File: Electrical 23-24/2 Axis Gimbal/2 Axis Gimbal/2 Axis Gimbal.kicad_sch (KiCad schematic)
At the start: 28 parts, among them IC1 BNO085, IC2 AP1086DL-13, J1 Conn_01x06_Socket, J2 Conn_01x06_Socket, U1 ATtiny404-SS

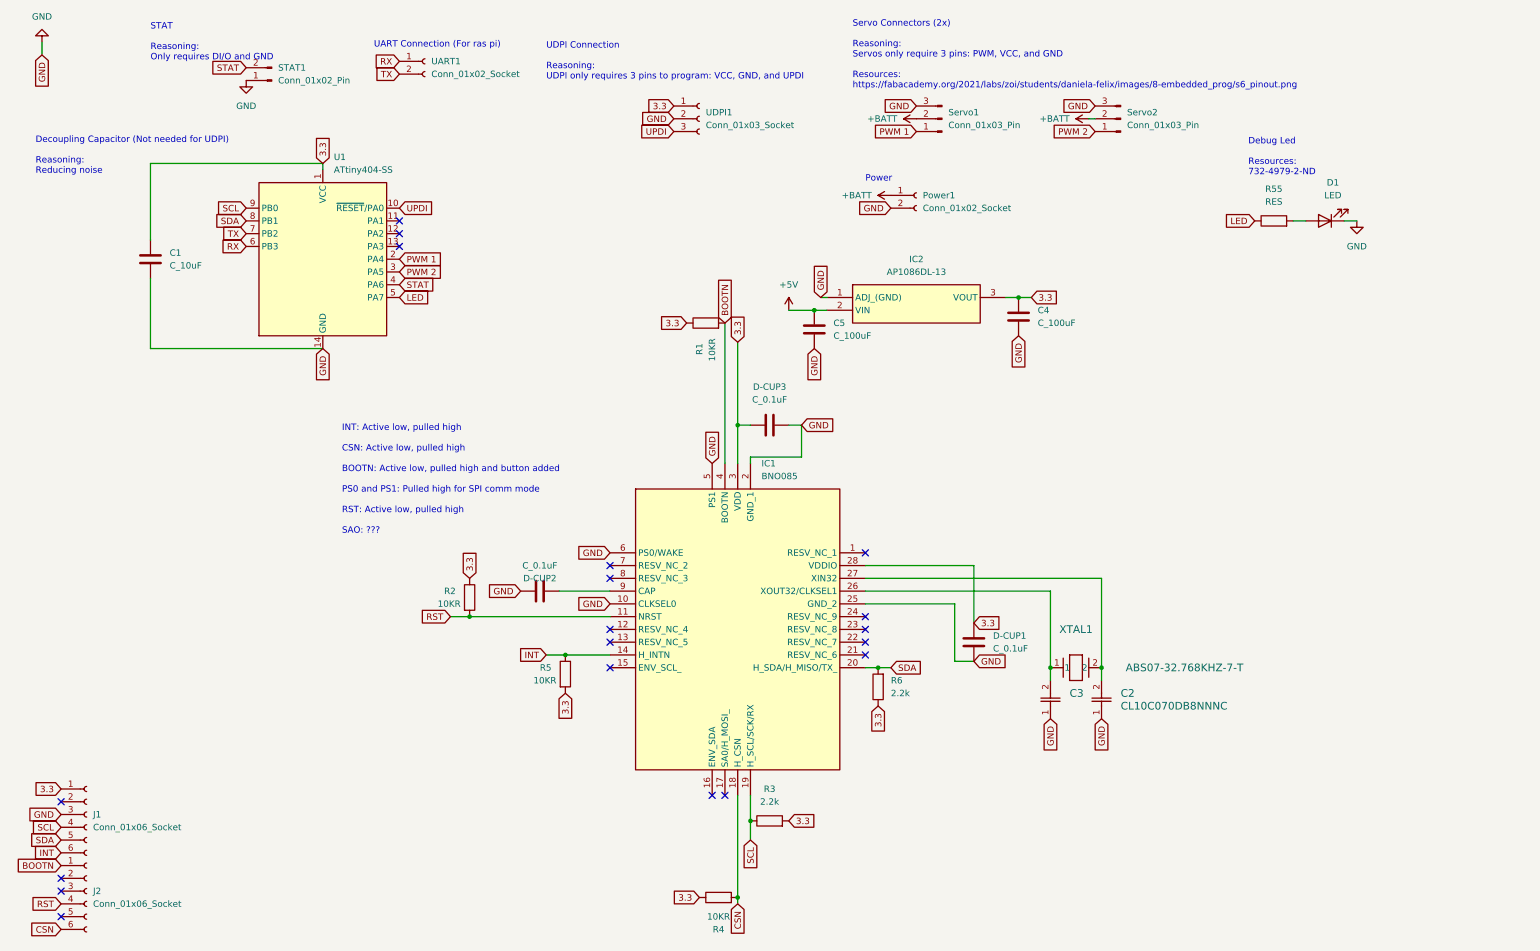
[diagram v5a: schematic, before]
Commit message: Fix gimbal schematic
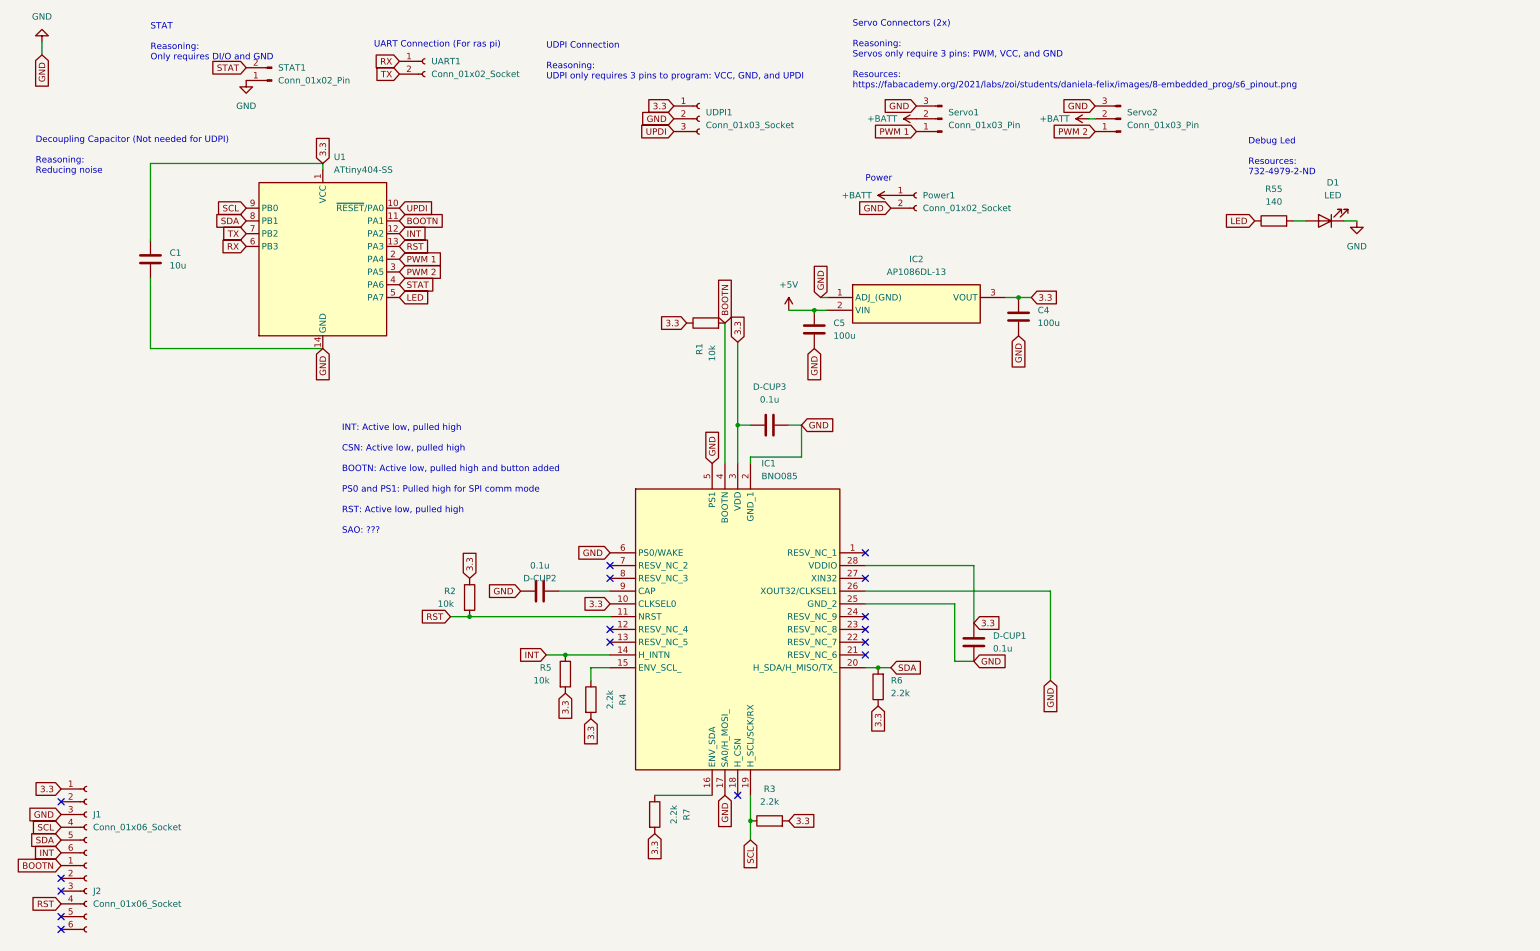
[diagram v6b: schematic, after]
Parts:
- removed C2, C3: CL10C070DB8NNNC, Capacitor_SMD:C_0201_0603Metric_Pad0.64x0.40mm_HandSolder, symbol 7pf:CL10C070DB8NNNC
- removed R4: 10KR, Resistor_SMD:R_0603_1608Metric_Pad0.98x0.95mm_HandSolder, symbol oem:10KR
- removed XTAL1: ABS07-32.768KHZ-7-T, 32Crys:XTAL_ABS07-32.768KHZ-7-T_ABR, symbol 32Crys:ABS07-32.768KHZ-7-T
- added R4, R7: 2.2k, Resistor_SMD:R_1206_3216Metric_Pad1.30x1.75mm_HandSolder, symbol Device:R
- C1: value C_10uF -> 10u
- C4, C5: value C_100uF -> 100u
- D-CUP1, D-CUP2, D-CUP3: value C_0.1uF -> 0.1u
- R1, R2, R5: value 10KR -> 10k
- R55: value RES -> 140
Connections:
- net 3.3: now also IC1.10 (CLKSEL0), R4.2, R7.2
- net BOOTN: now also U1.11 (PA1)
- net GND: now also IC1.17 (SA0/H_MOSI_), IC1.26 (XOUT32/CLKSEL1); no longer IC1.10 (CLKSEL0)
- net INT: now also U1.12 (PA2)
- net RST: now also U1.13 (PA3)
- net at IC1.15 (ENV_SCL_): now also R4.1
- net at IC1.16 (ENV_SDA): now also R7.1
- net CSN: no longer names the net of J2.6 (Pin_6)
- net CSN: no longer IC1.18 (H_CSN)
- no-connect marks 19 -> 16

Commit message: Finished Gimbal Board
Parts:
- removed J1, J2: Conn_01x06_Socket, Connector_PinHeader_2.54mm:PinHeader_1x06_P2.54mm_Vertical, symbol Connector:Conn_01x06_Socket
- removed UDPI1: Conn_01x03_Socket, Connector_PinSocket_2.54mm:PinSocket_1x03_P2.54mm_Vertical, symbol Connector:Conn_01x03_Socket
- added Servo3: Conn_01x03_Pin, Connector_JST:JST_XH_B3B-XH-A_1x03_P2.50mm_Vertical, symbol Connector:Conn_01x03_Pin
- added U2: ~, gimbal:breakout, symbol gimbal:breakout
- added UDPI1: Conn_01x03_Socket, Connector_PinSocket_2.54mm:PinSocket_1x05_P2.54mm_Vertical, symbol Connector:Conn_01x05_Socket
- C1: footprint Capacitor_SMD:C_0805_2012Metric_Pad1.18x1.45mm_HandSolder -> Capacitor_SMD:C_0603_1608Metric_Pad1.08x0.95mm_HandSolder
- C2: renamed from D-CUP2; footprint Capacitor_SMD:C_0402_1005Metric_Pad0.74x0.62mm_HandSolder -> Capacitor_SMD:C_0603_1608Metric_Pad1.08x0.95mm_HandSolder
- C3: renamed from D-CUP3; footprint Capacitor_SMD:C_0402_1005Metric_Pad0.74x0.62mm_HandSolder -> Capacitor_SMD:C_0603_1608Metric_Pad1.08x0.95mm_HandSolder
- C4, C5: value 100u -> 10u; footprint Capacitor_SMD:C_1206_3216Metric_Pad1.33x1.80mm_HandSolder -> Capacitor_SMD:C_0603_1608Metric_Pad1.08x0.95mm_HandSolder
- C6: renamed from D-CUP1; footprint Capacitor_SMD:C_0402_1005Metric_Pad0.74x0.62mm_HandSolder -> Capacitor_SMD:C_0603_1608Metric_Pad1.08x0.95mm_HandSolder
- IC1: footprint BNO085:BNO085 -> gimbal:BNO085
- IC2: footprint VReg3.3:TO252-3L_1 -> gimbal:TO252-3L_1
- Power1, UART1: footprint Connector_PinSocket_2.54mm:PinSocket_1x02_P2.54mm_Vertical -> Connector_JST:JST_XH_B2B-XH-A_1x02_P2.50mm_Vertical
- R1: footprint Resistor_SMD:R_0201_0603Metric_Pad0.64x0.40mm_HandSolder -> Resistor_SMD:R_0603_1608Metric_Pad0.98x0.95mm_HandSolder
- R3, R4, R6, R7: footprint Resistor_SMD:R_1206_3216Metric_Pad1.30x1.75mm_HandSolder -> Resistor_SMD:R_0603_1608Metric_Pad0.98x0.95mm_HandSolder
- R55: footprint LED_SMD:LED_1206_3216Metric_Pad1.42x1.75mm_HandSolder -> Resistor_SMD:R_0603_1608Metric_Pad0.98x0.95mm_HandSolder
- STAT1: footprint Connector_PinHeader_2.54mm:PinHeader_1x02_P2.54mm_Vertical -> Connector_JST:JST_XH_B2B-XH-A_1x02_P2.50mm_Vertical
- Servo1, Servo2: footprint Connector_PinHeader_2.54mm:PinHeader_1x03_P2.54mm_Vertical -> Connector_JST:JST_XH_B3B-XH-A_1x03_P2.50mm_Vertical
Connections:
- net +5V is gone; now on net +BATT: C5.1, IC2.2 (VIN)
- net +BATT: now also Servo3.2 (Pin_2)
- net 3.3: now also U2.1 (Vin), UDPI1.2 (Pin_2)
- net BOOTN: now also U2.12 (BT)
- net GND: now also Servo3.3 (Pin_3), U2.10 (P0), U2.11 (P1), U2.3 (GND), UDPI1.3 (Pin_3)
- net INT: now also U2.6 (Int)
- net PWM 1: now also U1.13 (PA3); no longer U1.2 (PA4)
- net PWM 2: now also U1.2 (PA4); no longer U1.3 (PA5)
- net RST: now also U1.5 (PA7), U2.9 (RST); no longer U1.13 (PA3)
- net RX: now also UDPI1.4 (Pin_4)
- net SCL: now also U2.4 (SCL)
- net SDA: now also U2.5 (SDA)
- net STAT: now also R55.1
- net TX: now also UDPI1.5 (Pin_5)
- net UPDI: now also UDPI1.1 (Pin_1)
- removed net LED: R55.1, U1.5 (PA7)
- new net PWM 3: Servo3.1 (Pin_1), U1.3 (PA5)
- no-connect marks 16 -> 14

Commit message: Fix a MAJOR issue that ANTHONY caused
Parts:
- added R8: 2.2k, Resistor_SMD:R_0603_1608Metric_Pad0.98x0.95mm_HandSolder, symbol Device:R
- added R9: 3.6k, Resistor_SMD:R_0603_1608Metric_Pad0.98x0.95mm_HandSolder, symbol Device:R
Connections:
- net 3.3: now also R8.2
- net GND: now also R9.1; no longer IC2.1 (ADJ_(GND))
- new net: IC2.1 (ADJ_(GND)), R8.1, R9.2
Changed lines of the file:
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@@
   (junction (at 156.21 95.25) (diameter 0) (color 0 0 0 0)
+  )
+  (junction (at 172.72 69.85) (diameter 0) (color 0 0 0 0)
   )
   (junction (at 121.92 140.97) (diameter 0) (color 0 0 0 0)
@@
     )
   )
-  (global_label "GND" (shape input) (at 172.72 69.85 90) (fields_autoplaced)
-    (effects (font (size 1.27 1.27)) (justify left))
-    (property "Intersheetrefs" "${INTERSHEET_REFS}" (at 172.72 62.9943 90)
-      (effects (font (size 1.27 1.27)) (justify left) hide)
-    )
-  )
   (global_label "RST" (shape input) (at 99.06 133.35 180) (fields_autoplaced)
     (effects (font (size 1.27 1.27)) (justify right))
@@
     )
   )
+  (global_label "GND" (shape input) (at 172.72 62.23 90) (fields_autoplaced)
+    (effects (font (size 1.27 1.27)) (justify left))
+    (property "Intersheetrefs" "${INTERSHEET_REFS}" (at 172.72 55.3743 90)
+      (effects (font (size 1.27 1.27)) (justify left) hide)
+    )
+  )
   (global_label "PWM 1" (shape input) (at 88.9 59.69 0) (fields_autoplaced)
     (effects (font (size 1.27 1.27)) (justify left))
@@
     (effects (font (size 1.27 1.27)) (justify right))
     (property "Intersheetrefs" "${INTERSHEET_REFS}" (at 106.1743 128.27 0)
+      (effects (font (size 1.27 1.27)) (justify right) hide)
+    )
+  )
+  (global_label "3.3" (shape input) (at 165.1 69.85 180) (fields_autoplaced)
+    (effects (font (size 1.27 1.27)) (justify right))
+    (property "Intersheetrefs" "${INTERSHEET_REFS}" (at 159.091 69.85 0)
       (effects (font (size 1.27 1.27)) (justify right) hide)
     )
@@
     )
   )
-  (symbol (lib_id "power:+BATT") (at 166.37 72.39 0) (unit 1)
-    (in_bom yes) (on_board yes) (dnp no) (fields_autoplaced)
-    (property "Reference" "#PWR03" (at 166.37 76.2 0)
-      (effects (font (size 1.27 1.27)) hide)
-    )
-    (property "Value" "+BATT" (at 166.37 67.31 0)
-      (effects (font (size 1.27 1.27)))
+  (symbol (lib_id "power:+BATT") (at 166.37 72.39 180) (unit 1)
+    (in_bom yes) (on_board yes) (dnp no)
+    (property "Reference" "#PWR03" (at 166.37 68.58 0)
+      (effects (font (size 1.27 1.27)) hide)
+    )
+    (property "Value" "+BATT" (at 162.56 76.2 0)
+      (effects (font (size 1.27 1.27)) (justify right))
     )
     (property "Footprint" "" (at 166.37 72.39 0)
@@
     )
   )
+  (symbol (lib_id "Device:R") (at 172.72 66.04 0) (unit 1)
+    (in_bom yes) (on_board yes) (dnp no) (fields_autoplaced)
+    (property "Reference" "R9" (at 175.26 64.77 0)
+      (effects (font (size 1.27 1.27)) (justify left))
+    )
+    (property "Value" "3.6k" (at 175.26 67.31 0)
+      (effects (font (size 1.27 1.27)) (justify left))
+    )
+    (property "Footprint" "Resistor_SMD:R_0603_1608Metric_Pad0.98x0.95mm_HandSolder" (at 170.942 66.04 90)
+      (effects (font (size 1.27 1.27)) hide)
+    )
+    (property "Datasheet" "~" (at 172.72 66.04 0)
+      (effects (font (size 1.27 1.27)) hide)
+    )
+    (pin "1")
+    (pin "2")
+    (instances
+      (project "2 Axis Gimbal"
+        (path "/b10b2b59-31cc-4d60-bc5f-41542c343df0"
+          (reference "R9") (unit 1)
+        )
+      )
+    )
+  )
   (symbol (lib_id "formula:C_10uF") (at 39.37 63.5 0) (unit 1)
     (in_bom yes) (on_board yes) (dnp no) (fields_autoplaced)
@@
         )
       )
+    )
+  )
+  (symbol (lib_id "Device:R") (at 168.91 69.85 270) (unit 1)
+    (in_bom yes) (on_board yes) (dnp no) (fields_autoplaced)
+    (property "Reference" "R8" (at 168.91 63.5 90)
+      (effects (font (size 1.27 1.27)))
+    )
+    (property "Value" "2.2k" (at 168.91 66.04 90)
+      (effects (font (size 1.27 1.27)))
+    )
+    (property "Footprint" "Resistor_SMD:R_0603_1608Metric_Pad0.98x0.95mm_HandSolder" (at 168.91 68.072 90)
+      (effects (font (size 1.27 1.27)) hide)
+    )
+    (property "Datasheet" "~" (at 168.91 69.85 0)
+      (effects (font (size 1.27 1.27)) hide)
+    )
+    (pin "1")
+    (pin "2")
+    (instances
+      (project "2 Axis Gimbal"
+        (path "/b10b2b59-31cc-4d60-bc5f-41542c343df0"
+          (reference "R8") (unit 1)
+        )
+      )
